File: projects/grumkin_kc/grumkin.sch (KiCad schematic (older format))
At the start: 0 parts

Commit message: Finishing the first version of the circuit
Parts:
- added CONN1: CONN_PWR_IN_5V, symbol CONN_PWR_IN_5V
- added CONN10, CONN11: CONN_RGB_IN, symbol CONN_RGB_IN
- added CONN2: CONN_PWR_OUT_5V, symbol CONN_PWR_OUT_5V
- added CONN20: LS_RGB0, symbol CONN_RGB_LEDSTRIP_OUT
- added CONN21: LS0, symbol CONN_LEDSTRIP_OUT
- added CONN22: LS1, symbol CONN_LEDSTRIP_OUT
- added CONN23: LS2, symbol CONN_LEDSTRIP_OUT
- added CONN24: LS_RGB3, symbol CONN_RGB_LEDSTRIP_OUT
- added CONN25: LS3, symbol CONN_LEDSTRIP_OUT
- added CONN26: LS4, symbol CONN_LEDSTRIP_OUT
- added CONN27: LS5, symbol CONN_LEDSTRIP_OUT
- added CONN3: CONN_PWR_IN_12V, symbol CONN_PWR_IN_12V
- added Q1, Q2, Q3, Q4, Q5, Q6: MOS_N, symbol MOS_N
- added R1, R2, R3, R4, R5, R6: 220, symbol R
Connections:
- new net: Q1.G, R1.1
- new net: CONN10.1 (R), R1.2
- new net: CONN20.2 (R), CONN21.2 (-), Q1.D
- new net: Q2.G, R2.1
- new net: CONN10.2 (G), R2.2
- new net: CONN20.3 (G), CONN22.2 (-), Q2.D
- new net: Q3.G, R3.1
- new net: CONN10.3 (B), R3.2
- new net: CONN20.4 (B), CONN23.2 (-), Q3.D
- new net: Q4.G, R4.1
- new net: CONN11.1 (R), R4.2
- new net: CONN24.2 (R), CONN25.2 (-), Q4.D
- new net: Q5.G, R5.1
- new net: CONN11.2 (G), R5.2
- new net: CONN24.3 (G), CONN26.2 (-), Q5.D
- new net: Q6.G, R6.1
- new net: CONN11.3 (B), R6.2
- new net: CONN24.4 (B), CONN27.2 (-), Q6.D
- new net +12V: CONN20.1 (+), CONN21.1 (+), CONN22.1 (+), CONN23.1 (+), CONN24.1 (+), CONN25.1 (+), CONN26.1 (+), CONN27.1 (+), CONN3.1 (+12V)
- new net +5V: CONN1.1 (+5V), CONN2.1 (+5V)
- new net GND: CONN1.2 (GND), CONN2.2 (GND), CONN3.2 (GND), Q1.S, Q2.S, Q3.S, Q4.S, Q5.S, Q6.S

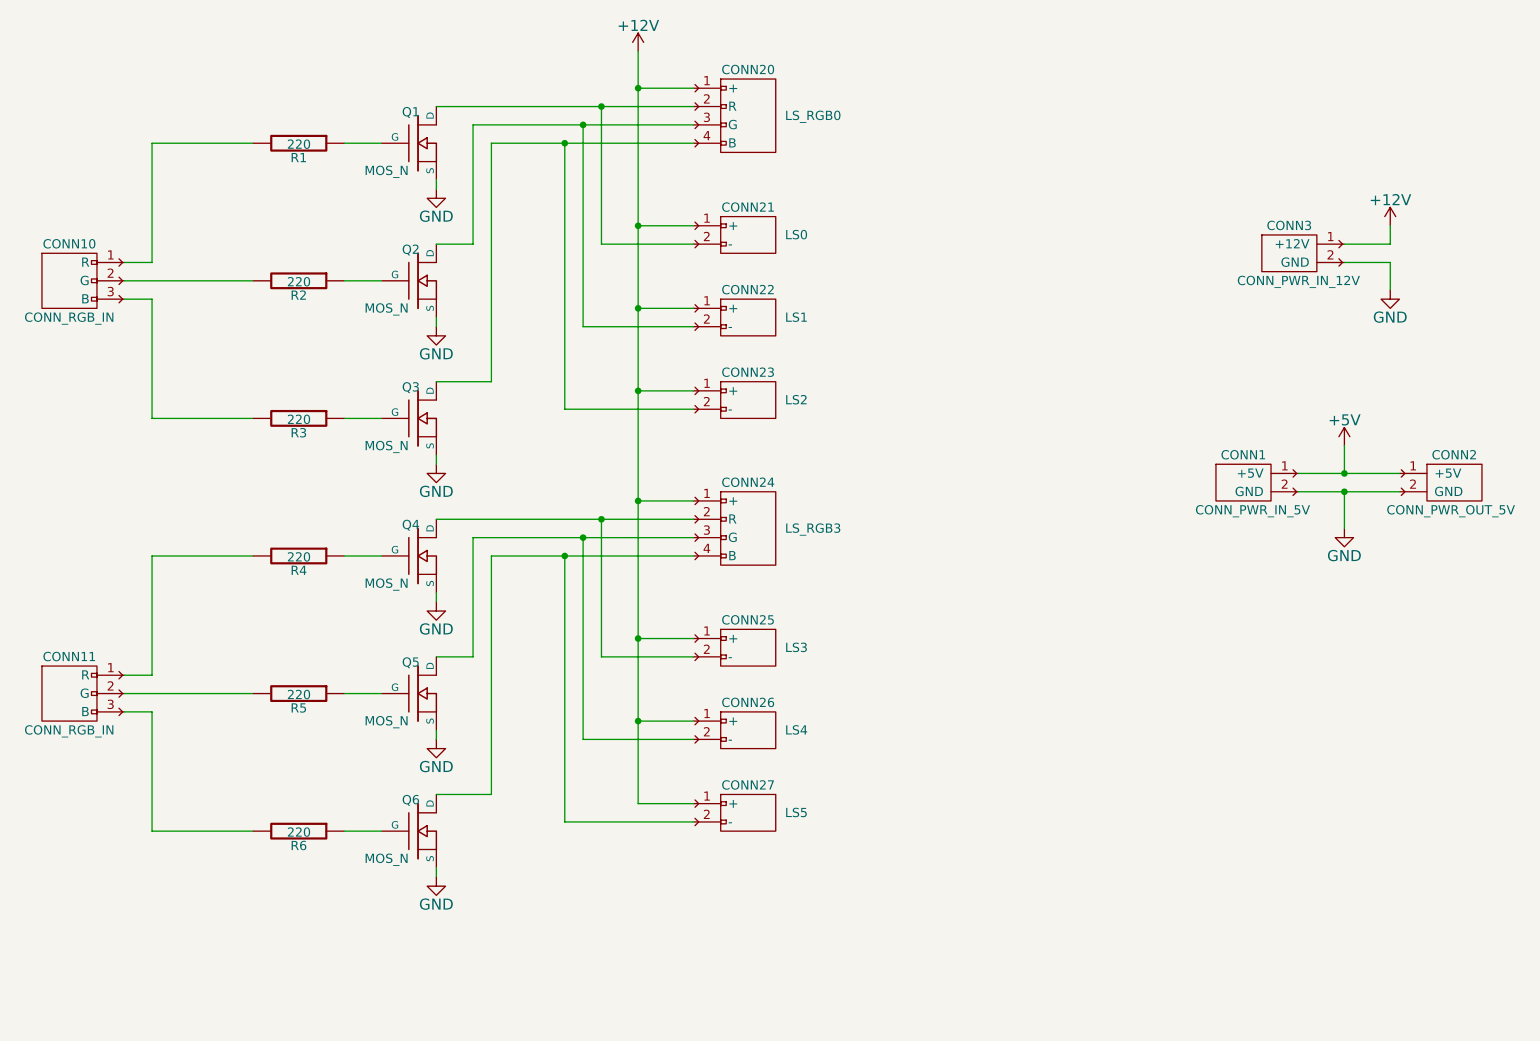
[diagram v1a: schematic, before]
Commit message: Adding indicator leds connector to schematics
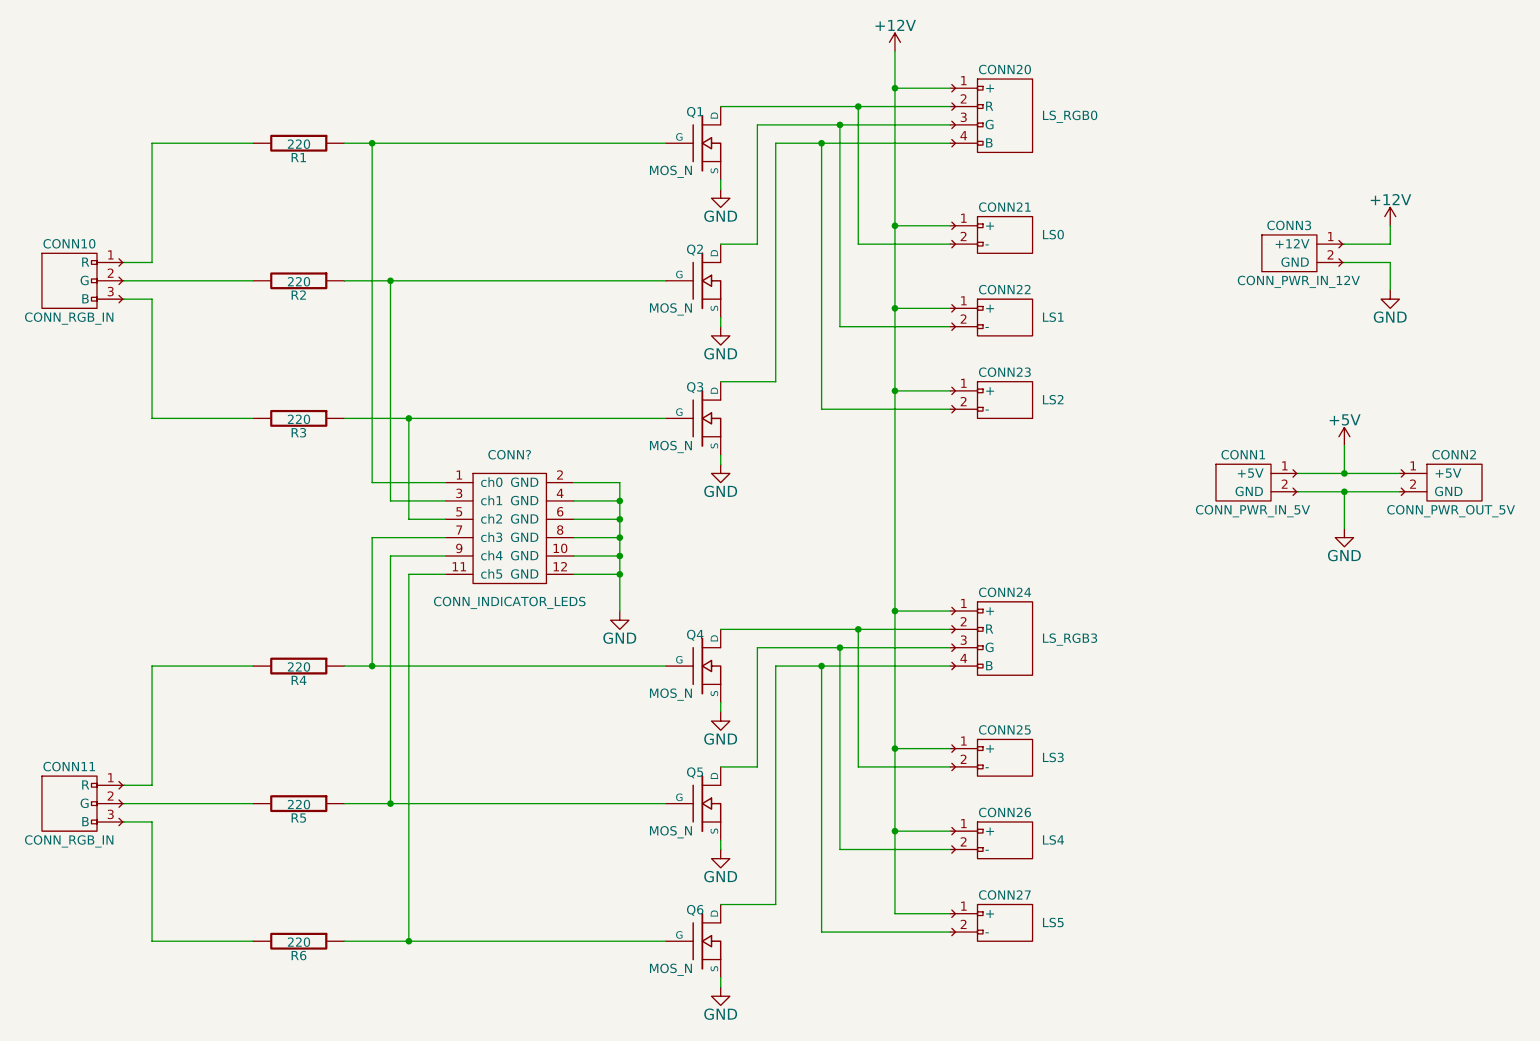
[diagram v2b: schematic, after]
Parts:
- added CONN?: CONN_INDICATOR_LEDS, symbol CONN_INDICATOR_LEDS
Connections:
- net GND: now also CONN?.10 (GND), CONN?.12 (GND), CONN?.2 (GND), CONN?.4 (GND), CONN?.6 (GND), CONN?.8 (GND)
- net at Q1.G, R1.1: now also CONN?.1 (ch0)
- net at Q2.G, R2.1: now also CONN?.3 (ch1)
- net at Q3.G, R3.1: now also CONN?.5 (ch2)
- net at Q4.G, R4.1: now also CONN?.7 (ch3)
- net at Q5.G, R5.1: now also CONN?.9 (ch4)
- net at Q6.G, R6.1: now also CONN?.11 (ch5)
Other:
- moved on the sheet: CONN11, CONN20, CONN21, CONN22, CONN23, CONN24, CONN25, CONN26, CONN27, Q1, Q2, Q3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

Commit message: Annotating components
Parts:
- gave numbers to parts that had none: 1
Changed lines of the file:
@@
 $EndComp
 $Comp
-L CONN_INDICATOR_LEDS CONN?
+L CONN_INDICATOR_LEDS CONN30
 U 1 1 54E4D00A
 P 3950 4000
-F 0 "CONN?" H 3950 4400 50  0000 C CNN
+F 0 "CONN30" H 3950 4400 50  0000 C CNN
 F 1 "CONN_INDICATOR_LEDS" H 3950 3600 50  0000 C CNN
 F 2 "" H 3900 4200 60  0000 C CNN
@@
 $EndComp
 $Comp
-L GND #PWR?
+L GND #PWR012
 U 1 1 54E4F245
 P 4550 4450
-F 0 "#PWR?" H 4550 4200 60  0001 C CNN
+F 0 "#PWR012" H 4550 4200 60  0001 C CNN
 F 1 "GND" H 4550 4300 60  0000 C CNN
 F 2 "" H 4550 4450 60  0000 C CNN

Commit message: Assigning footprints
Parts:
- CONN1, CONN2: footprint (none) -> pin_strip:pin_strip_2
- CONN10, CONN11: footprint (none) -> pin_strip:pin_strip_3
- CONN20, CONN24: footprint (none) -> conn_pt-1,5:pt_1,5-4-3,5-h
- CONN21, CONN22, CONN23, CONN25, CONN26, CONN27, CONN3: footprint (none) -> conn_pt-1,5:pt_1,5-2-3,5-h
- CONN30: footprint (none) -> pin_strip:pin_strip_6x2
- Q1, Q2, Q3, Q4, Q5, Q6: footprint (none) -> Transistors_TO-220:TO-220_Neutral123_Vertical
- R1, R2, R3, R4, R5, R6: footprint (none) -> Resistors_ThroughHole:Resistor_Horizontal_RM15mm
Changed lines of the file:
@@
 F 0 "R1" V 2880 1900 50  0000 C CNN
 F 1 "220" V 2807 1901 50  0000 C CNN
-F 2 "" V 2730 1900 30  0000 C CNN
+F 2 "Resistors_ThroughHole:Resistor_Horizontal_RM15mm" V 2730 1900 30  0001 C CNN
 F 3 "" H 2800 1900 30  0000 C CNN
 	1    2800 1900
@@
 F 0 "Q1" H 5010 2070 50  0000 R CNN
 F 1 "MOS_N" H 4950 1750 50  0000 R CNN
-F 2 "" H 5000 1900 60  0000 C CNN
+F 2 "Transistors_TO-220:TO-220_Neutral123_Vertical" H 5000 1900 60  0001 C CNN
 F 3 "" H 5000 1900 60  0000 C CNN
 	1    5000 1900
@@
 F 0 "R2" V 2880 2650 50  0000 C CNN
 F 1 "220" V 2807 2651 50  0000 C CNN
-F 2 "" V 2730 2650 30  0000 C CNN
+F 2 "Resistors_ThroughHole:Resistor_Horizontal_RM15mm" V 2730 2650 30  0001 C CNN
 F 3 "" H 2800 2650 30  0000 C CNN
 	1    2800 2650
@@
 F 0 "Q2" H 5010 2820 50  0000 R CNN
 F 1 "MOS_N" H 4950 2500 50  0000 R CNN
-F 2 "" H 5000 2650 60  0000 C CNN
+F 2 "Transistors_TO-220:TO-220_Neutral123_Vertical" H 5000 2650 60  0001 C CNN
 F 3 "" H 5000 2650 60  0000 C CNN
 	1    5000 2650
@@
 F 0 "R3" V 2880 3400 50  0000 C CNN
 F 1 "220" V 2807 3401 50  0000 C CNN
-F 2 "" V 2730 3400 30  0000 C CNN
+F 2 "Resistors_ThroughHole:Resistor_Horizontal_RM15mm" V 2730 3400 30  0001 C CNN
 F 3 "" H 2800 3400 30  0000 C CNN
 	1    2800 3400
@@
 F 0 "Q3" H 5010 3570 50  0000 R CNN
 F 1 "MOS_N" H 4950 3250 50  0000 R CNN
-F 2 "" H 5000 3400 60  0000 C CNN
+F 2 "Transistors_TO-220:TO-220_Neutral123_Vertical" H 5000 3400 60  0001 C CNN
 F 3 "" H 5000 3400 60  0000 C CNN
 	1    5000 3400
@@
 F 0 "R4" V 2880 4750 50  0000 C CNN
 F 1 "220" V 2807 4751 50  0000 C CNN
-F 2 "" V 2730 4750 30  0000 C CNN
+F 2 "Resistors_ThroughHole:Resistor_Horizontal_RM15mm" V 2730 4750 30  0001 C CNN
 F 3 "" H 2800 4750 30  0000 C CNN
 	1    2800 4750
@@
 F 0 "Q4" H 5010 4920 50  0000 R CNN
 F 1 "MOS_N" H 4950 4600 50  0000 R CNN
-F 2 "" H 5000 4750 60  0000 C CNN
+F 2 "Transistors_TO-220:TO-220_Neutral123_Vertical" H 5000 4750 60  0001 C CNN
 F 3 "" H 5000 4750 60  0000 C CNN
 	1    5000 4750
@@
 F 0 "R5" V 2880 5500 50  0000 C CNN
 F 1 "220" V 2807 5501 50  0000 C CNN
-F 2 "" V 2730 5500 30  0000 C CNN
+F 2 "Resistors_ThroughHole:Resistor_Horizontal_RM15mm" V 2730 5500 30  0001 C CNN
 F 3 "" H 2800 5500 30  0000 C CNN
 	1    2800 5500
@@
 F 0 "Q5" H 5010 5670 50  0000 R CNN
 F 1 "MOS_N" H 4950 5350 50  0000 R CNN
-F 2 "" H 5000 5500 60  0000 C CNN
+F 2 "Transistors_TO-220:TO-220_Neutral123_Vertical" H 5000 5500 60  0001 C CNN
 F 3 "" H 5000 5500 60  0000 C CNN
 	1    5000 5500
@@
 F 0 "R6" V 2880 6250 50  0000 C CNN
 F 1 "220" V 2807 6251 50  0000 C CNN
-F 2 "" V 2730 6250 30  0000 C CNN
+F 2 "Resistors_ThroughHole:Resistor_Horizontal_RM15mm" V 2730 6250 30  0001 C CNN
 F 3 "" H 2800 6250 30  0000 C CNN
 	1    2800 6250
@@
 F 0 "Q6" H 5010 6420 50  0000 R CNN
 F 1 "MOS_N" H 4950 6100 50  0000 R CNN
-F 2 "" H 5000 6250 60  0000 C CNN
+F 2 "Transistors_TO-220:TO-220_Neutral123_Vertical" H 5000 6250 60  0001 C CNN
 F 3 "" H 5000 6250 60  0000 C CNN
 	1    5000 6250
@@
 F 0 "CONN1" H 7950 3900 50  0000 C CNN
 F 1 "CONN_PWR_IN_5V" H 8000 3600 50  0000 C CNN
-F 2 "" H 7950 3750 60  0000 C CNN
+F 2 "pin_strip:pin_strip_2" H 7950 3750 60  0001 C CNN
 F 3 "" H 7950 3750 60  0000 C CNN
 	1    7950 3750
@@
 F 0 "CONN2" H 9100 3900 50  0000 C CNN
 F 1 "CONN_PWR_OUT_5V" H 9080 3600 50  0000 C CNN
-F 2 "" H 9100 3750 60  0000 C CNN
+F 2 "pin_strip:pin_strip_2" H 9100 3750 60  0001 C CNN
 F 3 "" H 9100 3750 60  0000 C CNN
 	1    9100 3750
@@
 F 0 "CONN10" H 1550 2850 50  0000 C CNN
 F 1 "CONN_RGB_IN" H 1550 2450 50  0000 C CNN
-F 2 "" H 1500 2700 60  0000 C CNN
+F 2 "pin_strip:pin_strip_3" H 1500 2700 60  0001 C CNN
 F 3 "" H 1500 2700 60  0000 C CNN
 	1    1550 2650
@@
 F 0 "CONN11" H 1550 5700 50  0000 C CNN
 F 1 "CONN_RGB_IN" H 1550 5300 50  0000 C CNN
-F 2 "" H 1500 5550 60  0000 C CNN
+F 2 "pin_strip:pin_strip_3" H 1500 5550 60  0001 C CNN
 F 3 "" H 1500 5550 60  0000 C CNN
 	1    1550 5500
@@
 F 0 "CONN20" H 6650 1900 50  0000 C CNN
 F 1 "LS_RGB0" H 6850 1650 50  0000 L CNN
-F 2 "" H 6600 1750 60  0000 C CNN
+F 2 "conn_pt-1,5:pt_1,5-4-3,5-h" H 6600 1750 60  0001 C CNN
 F 3 "" H 6600 1750 60  0000 C CNN
 	1    6650 1700
@@
 F 0 "CONN21" H 6650 2650 50  0000 C CNN
 F 1 "LS0" H 6850 2500 50  0000 L CNN
-F 2 "" H 6600 2500 60  0000 C CNN
+F 2 "conn_pt-1,5:pt_1,5-2-3,5-h" H 6600 2500 60  0001 C CNN
 F 3 "" H 6600 2500 60  0000 C CNN
 	1    6650 2450
@@
 F 0 "CONN22" H 6650 3100 50  0000 C CNN
 F 1 "LS1" H 6850 2950 50  0000 L CNN
-F 2 "" H 6600 2950 60  0000 C CNN
+F 2 "conn_pt-1,5:pt_1,5-2-3,5-h" H 6600 2950 60  0001 C CNN
 F 3 "" H 6600 2950 60  0000 C CNN
 	1    6650 2900
@@
 F 0 "CONN23" H 6650 3550 50  0000 C CNN
 F 1 "LS2" H 6850 3400 50  0000 L CNN
-F 2 "" H 6600 3400 60  0000 C CNN
+F 2 "conn_pt-1,5:pt_1,5-2-3,5-h" H 6600 3400 60  0001 C CNN
 F 3 "" H 6600 3400 60  0000 C CNN
 	1    6650 3350
@@
 F 0 "CONN24" H 6650 4750 50  0000 C CNN
 F 1 "LS_RGB3" H 6850 4500 50  0000 L CNN
-F 2 "" H 6600 4600 60  0000 C CNN
+F 2 "conn_pt-1,5:pt_1,5-4-3,5-h" H 6600 4600 60  0001 C CNN
 F 3 "" H 6600 4600 60  0000 C CNN
 	1    6650 4550
@@
 F 0 "CONN25" H 6650 5500 50  0000 C CNN
 F 1 "LS3" H 6850 5350 50  0000 L CNN
-F 2 "" H 6600 5350 60  0000 C CNN
+F 2 "conn_pt-1,5:pt_1,5-2-3,5-h" H 6600 5350 60  0001 C CNN
 F 3 "" H 6600 5350 60  0000 C CNN
 	1    6650 5300
@@
 F 0 "CONN26" H 6650 5950 50  0000 C CNN
 F 1 "LS4" H 6850 5800 50  0000 L CNN
-F 2 "" H 6600 5800 60  0000 C CNN
+F 2 "conn_pt-1,5:pt_1,5-2-3,5-h" H 6600 5800 60  0001 C CNN
 F 3 "" H 6600 5800 60  0000 C CNN
 	1    6650 5750
@@
 F 0 "CONN27" H 6650 6400 50  0000 C CNN
 F 1 "LS5" H 6850 6250 50  0000 L CNN
-F 2 "" H 6600 6250 60  0000 C CNN
+F 2 "conn_pt-1,5:pt_1,5-2-3,5-h" H 6600 6250 60  0001 C CNN
 F 3 "" H 6600 6250 60  0000 C CNN
 	1    6650 6200
@@
 F 0 "CONN3" H 8200 2650 50  0000 C CNN
 F 1 "CONN_PWR_IN_12V" H 8250 2350 50  0000 C CNN
-F 2 "" H 8200 2500 60  0000 C CNN
+F 2 "conn_pt-1,5:pt_1,5-2-3,5-h" H 8200 2500 60  0001 C CNN
 F 3 "" H 8200 2500 60  0000 C CNN
 	1    8200 2500
@@
 F 0 "CONN30" H 3950 4400 50  0000 C CNN
 F 1 "CONN_INDICATOR_LEDS" H 3950 3600 50  0000 C CNN
-F 2 "" H 3900 4200 60  0000 C CNN
+F 2 "pin_strip:pin_strip_6x2" H 3900 4200 60  0001 C CNN
 F 3 "" H 3900 4200 60  0000 C CNN
 	1    3950 4000

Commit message: Labeling LED_POWER lines
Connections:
- net LED_POWER: now reaches CONN20.2 (R), CONN21.2 (-), Q1.D
- net LED_POWER: now also CONN20.3 (G), CONN20.4 (B), CONN22.2 (-), CONN23.2 (-), CONN24.2 (R), CONN24.3 (G), CONN24.4 (B), CONN25.2 (-), CONN26.2 (-), CONN27.2 (-), Q2.D, Q3.D, Q4.D, Q5.D, Q6.D
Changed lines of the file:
@@
 Wire Wire Line
 	4550 3750 4550 4450
+Text Label 5300 1700 0    60   ~ 0
+LED_POWER
+Text Label 5350 1800 0    60   ~ 0
+LED_POWER
+Text Label 5400 1900 0    60   ~ 0
+LED_POWER
+Text Label 5300 4550 0    60   ~ 0
+LED_POWER
+Text Label 5350 4650 0    60   ~ 0
+LED_POWER
+Text Label 5400 4750 0    60   ~ 0
+LED_POWER
 $EndSCHEMATC

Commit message: Updating Indicator conector component and labeling LED power lines as such
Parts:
- Q1, Q2, Q3, Q4, Q5, Q6: footprint Transistors_TO-220:TO-220_Neutral123_Vertical -> Transistors_TO-220:TO-220_FET-GDS_Vertical
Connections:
- removed net LED_POWER: CONN20.2 (R), CONN20.3 (G), CONN20.4 (B), CONN21.2 (-), CONN22.2 (-), CONN23.2 (-), CONN24.2 (R), CONN24.3 (G), CONN24.4 (B), CONN25.2 (-), CONN26.2 (-), CONN27.2 (-), Q1.D, Q2.D, Q3.D, Q4.D, Q5.D, Q6.D
- new net LED_POWER_CH0: CONN20.2 (R), CONN21.2 (-), Q1.D
- new net LED_POWER_CH1: CONN20.3 (G), CONN22.2 (-), Q2.D
- new net LED_POWER_CH2: CONN20.4 (B), CONN23.2 (-), Q3.D
- new net LED_POWER_CH3: CONN24.2 (R), CONN25.2 (-), Q4.D
- new net LED_POWER_CH4: CONN24.3 (G), CONN26.2 (-), Q5.D
- new net LED_POWER_CH5: CONN24.4 (B), CONN27.2 (-), Q6.D
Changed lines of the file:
@@
 Title "Grumkin"
 Date ""
-Rev "0.1"
+Rev "0.4"
 Comp "Raging Bool"
 Comment1 "Grumkin: A 6-channel PWM LED driver"
@@
 F 0 "Q1" H 5010 2070 50  0000 R CNN
 F 1 "MOS_N" H 4950 1750 50  0000 R CNN
-F 2 "Transistors_TO-220:TO-220_Neutral123_Vertical" H 5000 1900 60  0001 C CNN
+F 2 "Transistors_TO-220:TO-220_FET-GDS_Vertical" H 5000 1900 60  0001 C CNN
 F 3 "" H 5000 1900 60  0000 C CNN
 	1    5000 1900
@@
 F 0 "Q2" H 5010 2820 50  0000 R CNN
 F 1 "MOS_N" H 4950 2500 50  0000 R CNN
-F 2 "Transistors_TO-220:TO-220_Neutral123_Vertical" H 5000 2650 60  0001 C CNN
+F 2 "Transistors_TO-220:TO-220_FET-GDS_Vertical" H 5000 2650 60  0001 C CNN
 F 3 "" H 5000 2650 60  0000 C CNN
 	1    5000 2650
@@
 F 0 "Q3" H 5010 3570 50  0000 R CNN
 F 1 "MOS_N" H 4950 3250 50  0000 R CNN
-F 2 "Transistors_TO-220:TO-220_Neutral123_Vertical" H 5000 3400 60  0001 C CNN
+F 2 "Transistors_TO-220:TO-220_FET-GDS_Vertical" H 5000 3400 60  0001 C CNN
 F 3 "" H 5000 3400 60  0000 C CNN
 	1    5000 3400
@@
 F 0 "Q4" H 5010 4920 50  0000 R CNN
 F 1 "MOS_N" H 4950 4600 50  0000 R CNN
-F 2 "Transistors_TO-220:TO-220_Neutral123_Vertical" H 5000 4750 60  0001 C CNN
+F 2 "Transistors_TO-220:TO-220_FET-GDS_Vertical" H 5000 4750 60  0001 C CNN
 F 3 "" H 5000 4750 60  0000 C CNN
 	1    5000 4750
@@
 F 0 "Q5" H 5010 5670 50  0000 R CNN
 F 1 "MOS_N" H 4950 5350 50  0000 R CNN
-F 2 "Transistors_TO-220:TO-220_Neutral123_Vertical" H 5000 5500 60  0001 C CNN
+F 2 "Transistors_TO-220:TO-220_FET-GDS_Vertical" H 5000 5500 60  0001 C CNN
 F 3 "" H 5000 5500 60  0000 C CNN
 	1    5000 5500
@@
 F 0 "Q6" H 5010 6420 50  0000 R CNN
 F 1 "MOS_N" H 4950 6100 50  0000 R CNN
-F 2 "Transistors_TO-220:TO-220_Neutral123_Vertical" H 5000 6250 60  0001 C CNN
+F 2 "Transistors_TO-220:TO-220_FET-GDS_Vertical" H 5000 6250 60  0001 C CNN
 F 3 "" H 5000 6250 60  0000 C CNN
 	1    5000 6250
@@
 $EndComp
 $Comp
-L CONN_INDICATOR_LEDS CONN30
-U 1 1 54E4D00A
-P 3950 4000
-F 0 "CONN30" H 3950 4400 50  0000 C CNN
-F 1 "CONN_INDICATOR_LEDS" H 3950 3600 50  0000 C CNN
-F 2 "pin_strip:pin_strip_6x2" H 3900 4200 60  0001 C CNN
-F 3 "" H 3900 4200 60  0000 C CNN
-	1    3950 4000
-	1    0    0    -1
-$EndComp
-$Comp
 L GND #PWR012
 U 1 1 54E4F245
@@
 	4550 3750 4550 4450
 Text Label 5300 1700 0    60   ~ 0
-LED_POWER
+LED_POWER_CH0
+Text Label 5300 4550 0    60   ~ 0
+LED_POWER_CH3
+Text Label 5350 4650 0    60   ~ 0
+LED_POWER_CH4
+Text Label 5400 4750 0    60   ~ 0
+LED_POWER_CH5
+$Comp
+L CONN_INDICATOR_LEDS CONN30
+U 1 1 54E51E5A
+P 3950 4000
+F 0 "CONN30" H 3950 4400 50  0000 C CNN
+F 1 "CONN_INDICATOR_LEDS" H 3950 3600 50  0000 C CNN
+F 2 "pin_strip:pin_strip_6x2" H 3900 4200 60  0001 C CNN
+F 3 "" H 3900 4200 60  0000 C CNN
+	1    3950 4000
+	1    0    0    -1
+$EndComp
+Text Label 5400 1900 0    60   ~ 0
+LED_POWER_CH2
 Text Label 5350 1800 0    60   ~ 0
-LED_POWER
-Text Label 5400 1900 0    60   ~ 0
-LED_POWER
-Text Label 5300 4550 0    60   ~ 0
-LED_POWER
-Text Label 5350 4650 0    60   ~ 0
-LED_POWER
-Text Label 5400 4750 0    60   ~ 0
-LED_POWER
+LED_POWER_CH1
 $EndSCHEMATC
